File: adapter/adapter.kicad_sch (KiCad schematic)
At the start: 26 parts, among them J1 Serial, J2 Ribbon, J3 RGB, J4 Ribbon, J5 Battery charge, SW1 SW_SPST, SW3 SW_SPDT, U1 Dual MCU: RP2040 + nice!nano, U2 AP1603WG-7

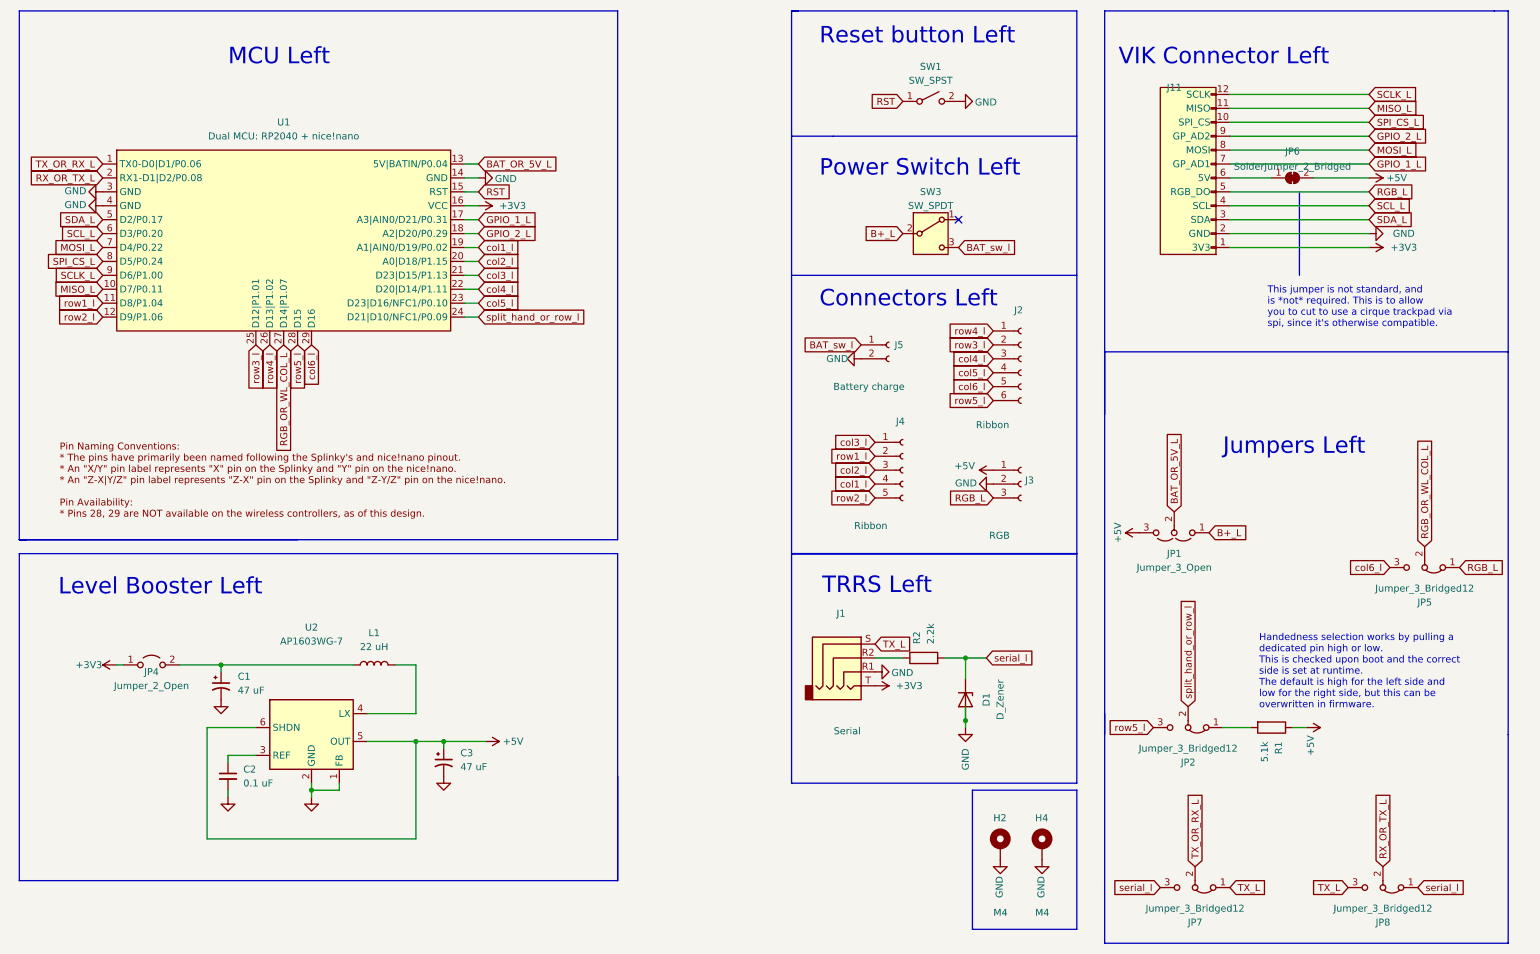
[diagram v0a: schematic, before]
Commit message: sch: move (potential) RGB pin to a high freq pin & CS to a low freq pin
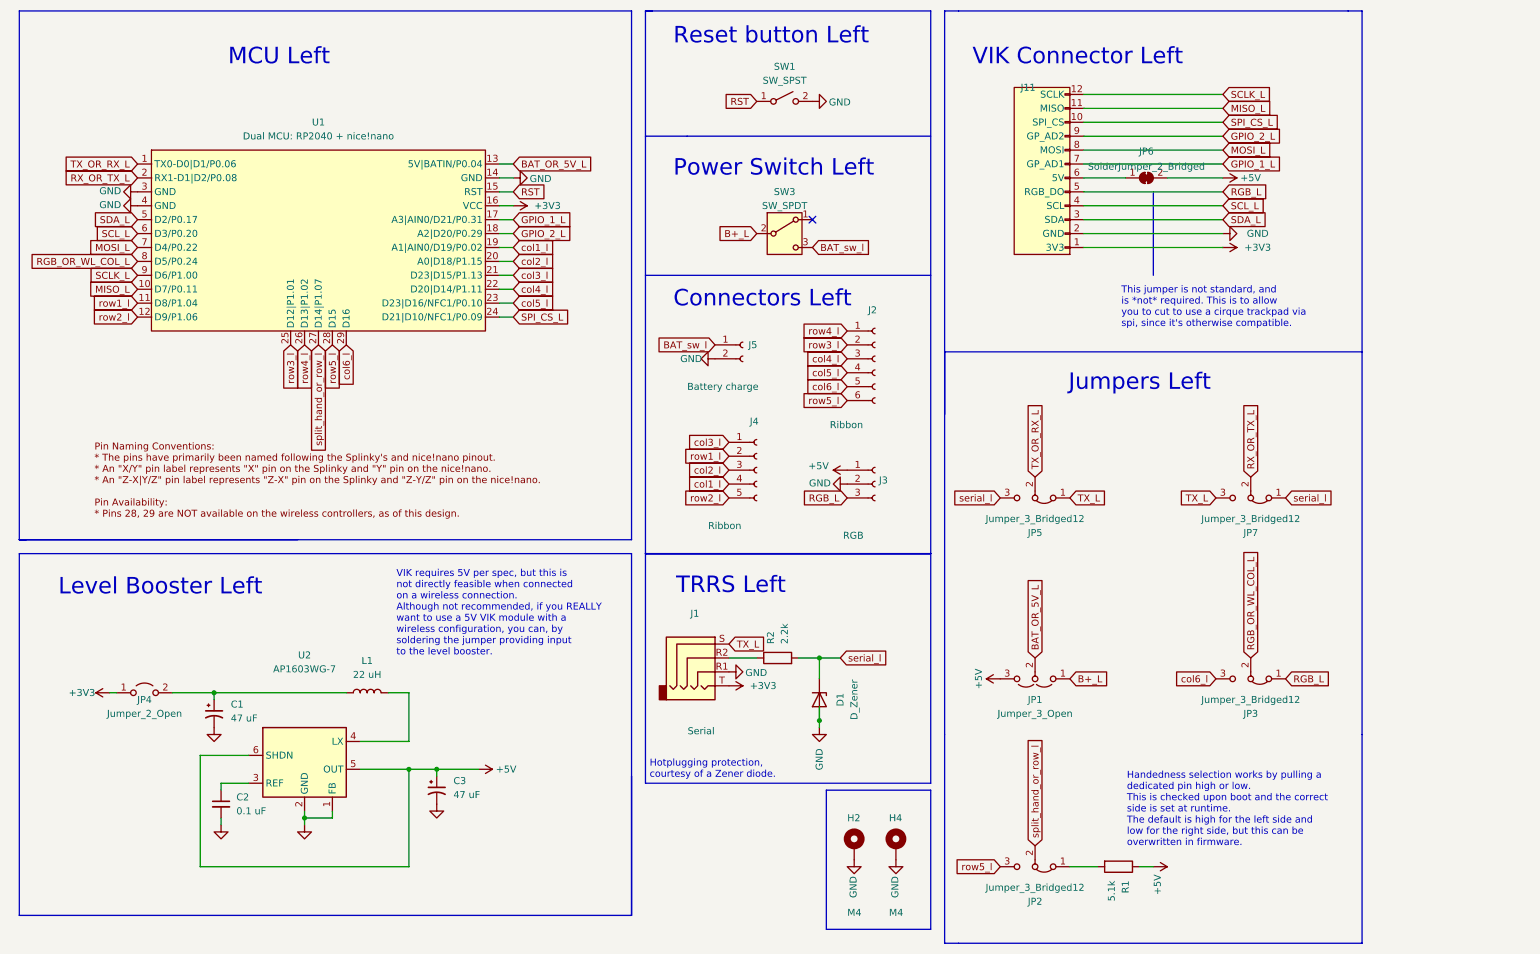
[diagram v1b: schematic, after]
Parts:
- removed JP8: Jumper_3_Bridged12, Jumper:SolderJumper-3_P1.3mm_Bridged12_RoundedPad1.0x1.5mm_NumberLabels, symbol Jumper:Jumper_3_Bridged12
- added JP3: Jumper_3_Bridged12, Jumper:SolderJumper-3_P1.3mm_Bridged12_RoundedPad1.0x1.5mm_NumberLabels, symbol Jumper:Jumper_3_Bridged12
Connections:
- net RGB_L: now also JP3.1 (A); no longer JP5.1 (A)
- net RGB_OR_WL_COL_L: now also U1.8 (D5/P0.24), JP3.2 (C); no longer JP5.2 (C), U1.27 (D14|P1.07)
- net RX_OR_TX_L: now also JP7.2 (C)
- net SPI_CS_L: now also U1.24 (D21|D10/NFC1/P0.09); no longer U1.8 (D5/P0.24)
- net TX_L: now also JP5.1 (A), JP7.3 (B); no longer JP7.1 (A)
- net TX_OR_RX_L: now also JP5.2 (C); no longer JP7.2 (C)
- net col6_l: now also JP3.3 (B); no longer JP5.3 (B)
- net serial_l: now also JP5.3 (B), JP7.1 (A); no longer JP7.3 (B)
- net split_hand_or_row_l: now also U1.27 (D14|P1.07); no longer U1.24 (D21|D10/NFC1/P0.09)
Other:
- note added: "Hotplugging protection, courtesy of a Zener diode."
- note added: "VIK requires 5V per spec, but this is not directly feasible when connected on a wireless connection. Although not recommended, if you REALLY want to use a 5V VIK module with a wireless configuration, you can, by soldering the jumper providing input to the level booster."
- moved on the sheet: C1, C2, C3, D1, H2, H4, J1, J11, J2, J3, J4, J5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

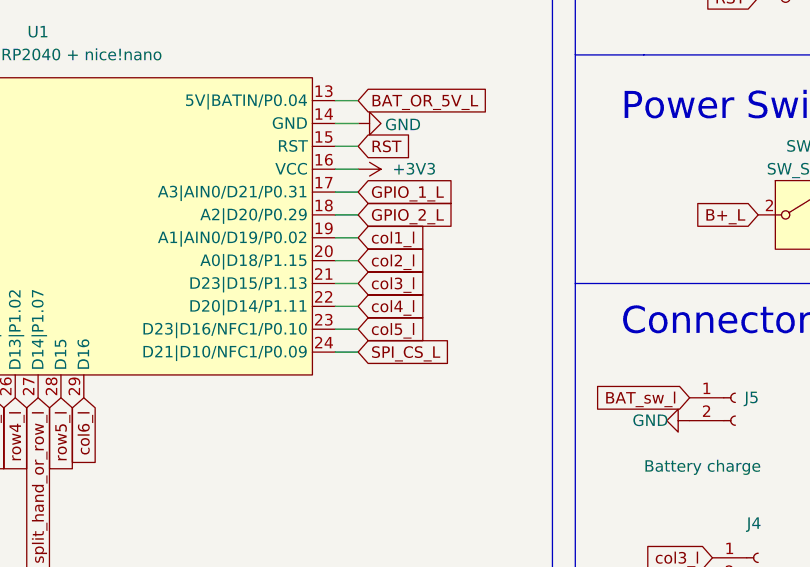
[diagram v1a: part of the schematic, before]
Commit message: pcb: wire up col and row pins
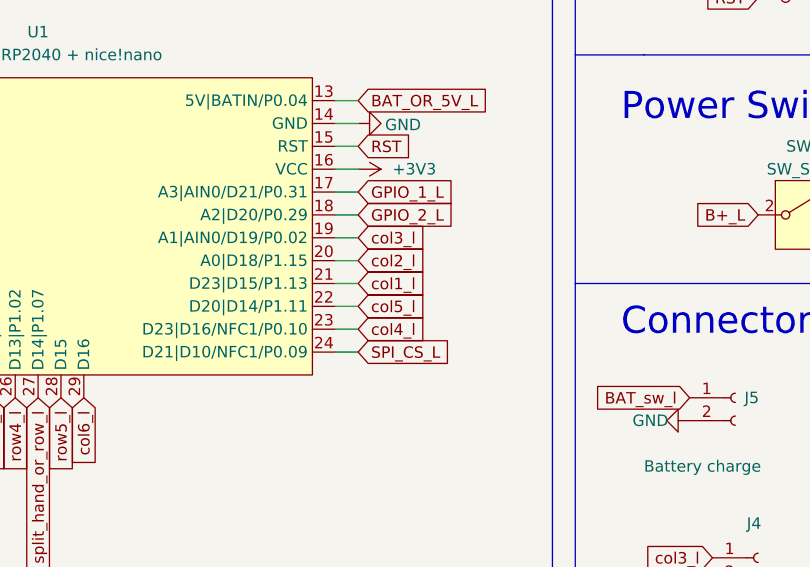
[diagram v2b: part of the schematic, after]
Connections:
- net col1_l: now also U1.21 (D23|D15/P1.13); no longer U1.19 (A1|AIN0/D19/P0.02)
- net col3_l: now also U1.19 (A1|AIN0/D19/P0.02); no longer U1.21 (D23|D15/P1.13)
- net col4_l: now also U1.23 (D23|D16/NFC1/P0.10); no longer U1.22 (D20|D14/P1.11)
- net col5_l: now also U1.22 (D20|D14/P1.11); no longer U1.23 (D23|D16/NFC1/P0.10)
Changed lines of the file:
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@@
-		)
-	)
-	(global_label "col5_l"
-		(shape input)
-		(at 102.87 66.04 0)
-		(effects
-			(font
-				(size 1.27 1.27)
-			)
-			(justify left)
-		)
-		(property "Intersheetrefs" "${INTERSHEET_REFS}"
-			(at 132.08 128.27 0)
-			(effects
-				(font
-					(size 1.27 1.27)
-				)
-				(hide yes)
-			)
 		)
 	)
@@
 		)
 	)
-	(global_label "col3_l"
-		(shape input)
-		(at 102.87 60.96 0)
-		(effects
-			(font
-				(size 1.27 1.27)
-			)
-			(justify left)
-		)
-		(property "Intersheetrefs" "${INTERSHEET_REFS}"
-			(at 132.08 100.33 0)
-			(effects
-				(font
-					(size 1.27 1.27)
-				)
-				(hide yes)
-			)
-		)
-	)
 	(global_label "SCL_L"
 		(shape input)
@@
 		)
 	)
+	(global_label "col1_l"
+		(shape input)
+		(at 102.87 60.96 0)
+		(effects
+			(font
+				(size 1.27 1.27)
+			)
+			(justify left)
+		)
+		(property "Intersheetrefs" "${INTERSHEET_REFS}"
+			(at 132.08 107.95 0)
+			(effects
+				(font
+					(size 1.27 1.27)
+				)
+				(hide yes)
+			)
+		)
+	)
 	(global_label "SPI_CS_L"
 		(shape input)
@@
 		(property "Intersheetrefs" "${INTERSHEET_REFS}"
 			(at 113.03 52.07 0)
+			(effects
+				(font
+					(size 1.27 1.27)
+				)
+				(hide yes)
+			)
+		)
+	)
+	(global_label "col5_l"
+		(shape input)
+		(at 102.87 63.5 0)
+		(effects
+			(font
+				(size 1.27 1.27)
+			)
+			(justify left)
+		)
+		(property "Intersheetrefs" "${INTERSHEET_REFS}"
+			(at 132.08 125.73 0)
 			(effects
 				(font
@@
 		)
 	)
+	(global_label "col3_l"
+		(shape input)
+		(at 102.87 55.88 0)
+		(effects
+			(font
+				(size 1.27 1.27)
+			)
+			(justify left)
+		)
+		(property "Intersheetrefs" "${INTERSHEET_REFS}"
+			(at 132.08 95.25 0)
+			(effects
+				(font
+					(size 1.27 1.27)
+				)
+				(hide yes)
+			)
+		)
+	)
 	(global_label "GPIO_2_L"
 		(shape input)
@@
 		)
 	)
+	(global_label "col2_l"
+		(shape input)
+		(at 142.24 96.52 180)
+		(effects
+			(font
+				(size 1.27 1.27)
+			)
+			(justify right)
+		)
+		(property "Intersheetrefs" "${INTERSHEET_REFS}"
+			(at 113.03 52.07 0)
+			(effects
+				(font
+					(size 1.27 1.27)
+				)
+				(hide yes)
+			)
+		)
+	)
+	(global_label "row4_l"
+		(shape input)
+		(at 163.83 71.12 180)
+		(effects
+			(font
+				(size 1.27 1.27)
+			)
+			(justify right)
+		)
+		(property "Intersheetrefs" "${INTERSHEET_REFS}"
+			(at 134.62 16.51 0)
+			(effects
+				(font
+					(size 1.27 1.27)
+				)
+				(hide yes)
+			)
+		)
+	)
+	(global_label "row5_l"
+		(shape input)
+		(at 191.77 168.91 180)
+		(effects
+			(font
+				(size 1.27 1.27)
+			)
+			(justify right)
+		)
+		(property "Intersheetrefs" "${INTERSHEET_REFS}"
+			(at 162.56 101.6 0)
+			(effects
+				(font
+					(size 1.27 1.27)
+				)
+				(hide yes)
+			)
+		)
+	)
 	(global_label "col4_l"
 		(shape input)
-		(at 102.87 63.5 0)
-		(effects
-			(font
-				(size 1.27 1.27)
-			)
-			(justify left)
-		)
-		(property "Intersheetrefs" "${INTERSHEET_REFS}"
-			(at 132.08 123.19 0)
-			(effects
-				(font
-					(size 1.27 1.27)
-				)
-				(hide yes)
-			)
-		)
-	)
-	(global_label "col2_l"
-		(shape input)
-		(at 142.24 96.52 180)
-		(effects
-			(font
-				(size 1.27 1.27)
-			)
-			(justify right)
-		)
-		(property "Intersheetrefs" "${INTERSHEET_REFS}"
-			(at 113.03 52.07 0)
-			(effects
-				(font
-					(size 1.27 1.27)
-				)
-				(hide yes)
-			)
-		)
-	)
-	(global_label "row4_l"
-		(shape input)
-		(at 163.83 71.12 180)
-		(effects
-			(font
-				(size 1.27 1.27)
-			)
-			(justify right)
-		)
-		(property "Intersheetrefs" "${INTERSHEET_REFS}"
-			(at 134.62 16.51 0)
-			(effects
-				(font
-					(size 1.27 1.27)
-				)
-				(hide yes)
-			)
-		)
-	)
-	(global_label "row5_l"
-		(shape input)
-		(at 191.77 168.91 180)
-		(effects
-			(font
-				(size 1.27 1.27)
-			)
-			(justify right)
-		)
-		(property "Intersheetrefs" "${INTERSHEET_REFS}"
-			(at 162.56 101.6 0)
+		(at 102.87 66.04 0)
+		(effects
+			(font
+				(size 1.27 1.27)
+			)
+			(justify left)
+		)
+		(property "Intersheetrefs" "${INTERSHEET_REFS}"
+			(at 132.08 125.73 0)
 			(effects
 				(font
@@
 			(effects
 				(font
-					(size 1.27 1.27)
-				)
-				(hide yes)
-			)
-		)
-	)
-	(global_label "col1_l"
-		(shape input)
-		(at 102.87 55.88 0)
-		(effects
-			(font
-				(size 1.27 1.27)
-			)
-			(justify left)
-		)
-		(property "Intersheetrefs" "${INTERSHEET_REFS}"
-			(at 132.08 102.87 0)
-			(effects
-				(font

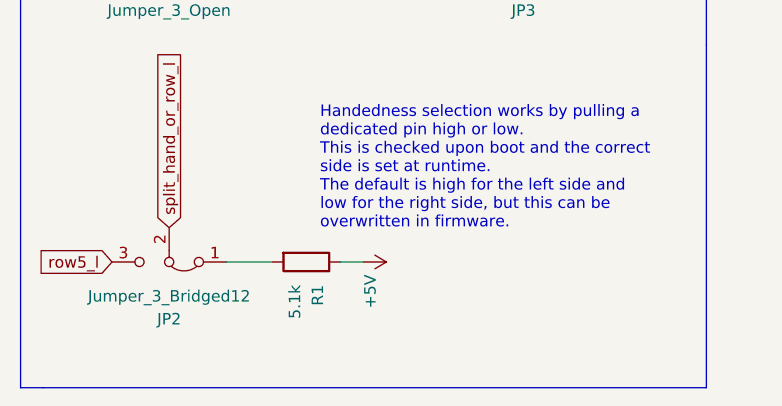
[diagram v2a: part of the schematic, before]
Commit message: sch: pull up left-handedness with 3.3v
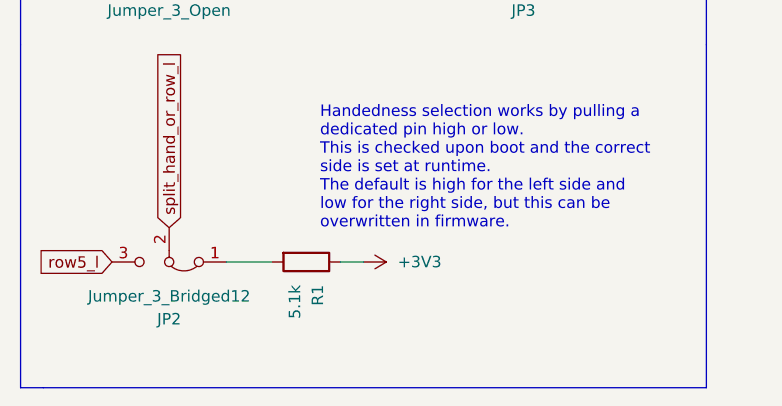
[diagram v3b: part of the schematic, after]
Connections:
- net +3V3: now also R1.1
- net +5V: no longer R1.1
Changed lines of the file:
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@@
+	)
+	(symbol
+		(lib_id "power:+5V")
+		(at 219.71 168.91 270)
+		(unit 1)
+		(exclude_from_sim no)
+		(in_bom yes)
+		(on_board yes)
+		(dnp no)
+		(property "Reference" "#PWR07"
+			(at 215.9 168.91 0)
+			(effects
+				(font
+					(size 1.27 1.27)
+				)
+				(hide yes)
+			)
+		)
+		(property "Value" "+3V3"
+			(at 223.52 168.9099 90)
+			(effects
+				(font
+					(size 1.27 1.27)
+				)
+				(justify left)
+			)
+		)
+		(property "Footprint" ""
+			(at 219.71 168.91 0)
+			(effects
+				(font
+					(size 1.27 1.27)
+				)
+				(hide yes)
+			)
+		)
+		(property "Datasheet" ""
+			(at 219.71 168.91 0)
+			(effects
+				(font
+					(size 1.27 1.27)
+				)
+				(hide yes)
+			)
+		)
+		(property "Description" "Power symbol creates a global label with name \"+5V\""
+			(at 219.71 168.91 0)
+			(effects
+				(font
+					(size 1.27 1.27)
+				)
+				(hide yes)
+			)
+		)
+		(pin "1"
+		)
+		(instances
+			(project "adapter"
+				(path "/e63e39d7-6ac0-4ffd-8aa3-1841a4541b55"
+					(reference "#PWR07")
+					(unit 1)
+				)
+			)
+		)
 	)
 	(symbol
@@
 					(unit 1)
 				)
-			)
-		)
-	)
-	(symbol
-		(lib_id "power:+5V")
-		(at 219.71 168.91 270)
-		(unit 1)
-		(exclude_from_sim no)
-		(in_bom yes)
-		(on_board yes)
-		(dnp no)
-		(property "Reference" "#PWR07"
-			(at 215.9 168.91 0)
-			(effects
-				(font
-					(size 1.27 1.27)
-				)
-				(hide yes)
-			)
-		)
-		(property "Value" "+5V"
-			(at 220.472 170.307 0)
-			(effects
-				(font
-					(size 1.27 1.27)
-				)
-				(justify left)
-			)
-		)
-		(property "Footprint" ""
-			(at 219.71 168.91 0)
-			(effects
-				(font
-					(size 1.27 1.27)
-				)
-				(hide yes)
-			)
-		)
-		(property "Datasheet" ""
-			(at 219.71 168.91 0)
-			(effects
-				(font
-					(size 1.27 1.27)
-				)
-				(hide yes)
-			)
-		)
-		(property "Description" "Power symbol creates a global label with name \"+5V\""
-			(at 219.71 168.91 0)
-			(effects
-				(font
-					(size 1.27 1.27)
-				)
-				(hide yes)
-			)
-		)
-		(pin "1"
-		)
-		(instances
-			(project "adapter"
-				(path "/e63e39d7-6ac0-4ffd-8aa3-1841a4541b55"
-					(reference "#PWR07")
-					(unit 1)
-				)

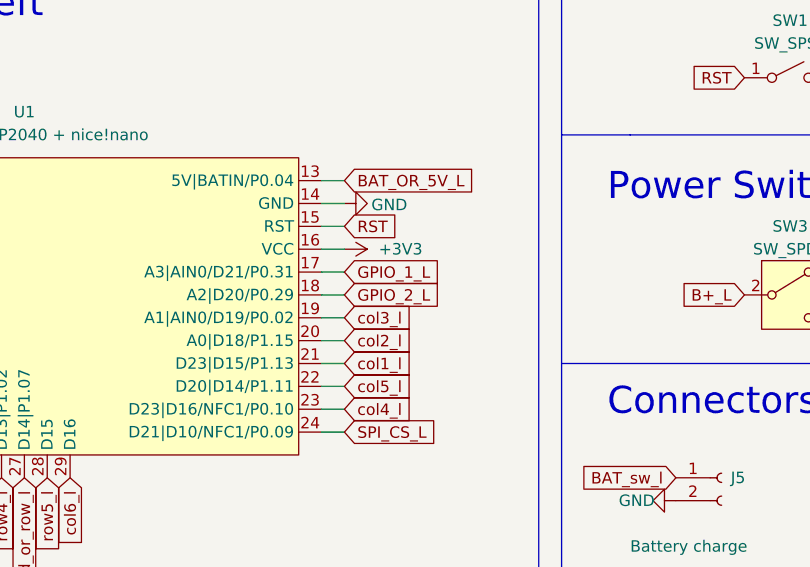
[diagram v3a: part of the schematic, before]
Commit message: pcb: route vik gpios
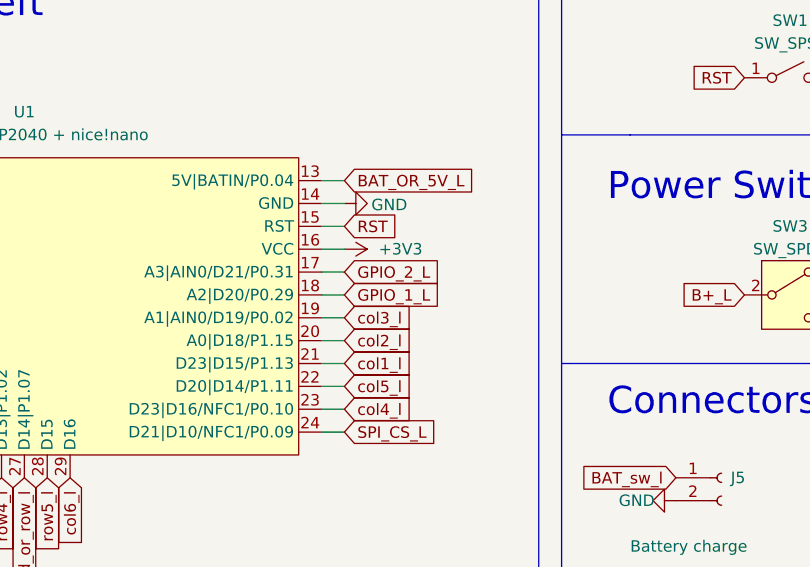
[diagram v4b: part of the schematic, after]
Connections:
- net GPIO_1_L: now also U1.18 (A2|D20/P0.29); no longer U1.17 (A3|AIN0/D21/P0.31)
- net GPIO_2_L: now also U1.17 (A3|AIN0/D21/P0.31); no longer U1.18 (A2|D20/P0.29)
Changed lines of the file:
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@@
+		)
+	)
+	(global_label "GPIO_2_L"
+		(shape input)
+		(at 102.87 50.8 0)
+		(effects
+			(font
+				(size 1.27 1.27)
+			)
+			(justify left)
+		)
+		(property "Intersheetrefs" "${INTERSHEET_REFS}"
+			(at 132.08 97.79 0)
+			(effects
+				(font
+					(size 1.27 1.27)
+				)
+				(hide yes)
+			)
 		)
 	)
@@
 	(global_label "GPIO_1_L"
 		(shape input)
-		(at 102.87 50.8 0)
-		(effects
-			(font
-				(size 1.27 1.27)
-			)
-			(justify left)
-		)
-		(property "Intersheetrefs" "${INTERSHEET_REFS}"
-			(at 132.08 97.79 0)
+		(at 102.87 53.34 0)
+		(effects
+			(font
+				(size 1.27 1.27)
+			)
+			(justify left)
+		)
+		(property "Intersheetrefs" "${INTERSHEET_REFS}"
+			(at 132.08 100.33 0)
 			(effects
 				(font
@@
 				(hide yes)
 			)
-		)
-	)
-	(global_label "GPIO_2_L"
-		(shape input)
-		(at 102.87 53.34 0)
-		(effects
-			(font
-				(size 1.27 1.27)
-			)
-			(justify left)
-		)
-		(property "Intersheetrefs" "${INTERSHEET_REFS}"
-			(at 132.08 100.33 0)
-			(effects
-				(font
-					(size 1.27 1.27)
-				)
-				(hide yes)
-			)

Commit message: pcb: 3d model for tactile reset switch
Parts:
- J5: footprint library:PinHeader_1x02_P2.54mm_Vertical -> Connector_JST:JST_PH_S2B-PH-K_1x02_P2.00mm_Horizontal
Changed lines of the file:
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@@
 			)
 		)
-		(property "Footprint" "library:PinHeader_1x02_P2.54mm_Vertical"
+		(property "Footprint" "Connector_JST:JST_PH_S2B-PH-K_1x02_P2.00mm_Horizontal"
 			(at 144.78 73.66 0)
 			(effects

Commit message: pcb: make level booster circuit components all 0805 size
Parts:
- C1, C3: footprint Capacitor_SMD:C_0603_1608Metric -> Capacitor_SMD:C_0805_2012Metric
- C2: footprint Capacitor_SMD:C_0402_1005Metric -> Capacitor_SMD:C_0805_2012Metric
- L1: footprint Inductor_SMD:L_0603_1608Metric -> Inductor_SMD:L_0805_2012Metric
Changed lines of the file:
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@@
 			)
 		)
-		(property "Footprint" "Capacitor_SMD:C_0603_1608Metric"
+		(property "Footprint" "Capacitor_SMD:C_0805_2012Metric"
 			(at 48.26 140.97 0)
 			(effects
@@
 			)
 		)
-		(property "Footprint" "Inductor_SMD:L_0603_1608Metric"
+		(property "Footprint" "Inductor_SMD:L_0805_2012Metric"
 			(at 76.2 137.16 0)
 			(effects
@@
 			)
 		)
-		(property "Footprint" "Capacitor_SMD:C_0603_1608Metric"
+		(property "Footprint" "Capacitor_SMD:C_0805_2012Metric"
 			(at 88.9 154.94 0)
 			(effects
@@
 			)
 		)
-		(property "Footprint" "Capacitor_SMD:C_0402_1005Metric"
+		(property "Footprint" "Capacitor_SMD:C_0805_2012Metric"
 			(at 49.53 157.48 0)
 			(effects

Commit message: pcb: fix drc
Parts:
- JP1: footprint (none) -> Jumper:SolderJumper-3_P1.3mm_Open_RoundedPad1.0x1.5mm
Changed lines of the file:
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@@
 			)
 		)
-		(property "Footprint" ""
+		(property "Footprint" "Jumper:SolderJumper-3_P1.3mm_Open_RoundedPad1.0x1.5mm"
 			(at 198.12 134.62 0)
 			(effects
